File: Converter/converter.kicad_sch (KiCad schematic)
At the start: 0 parts

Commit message: added more flesh to overall structure, primarily on converter stage
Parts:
- added C10, C5, C6, C7, C8, C9, C_{bulk,in}, C_{bulk,out}: ~, symbol Device:C
- added L1: L, symbol Device:L
- added Q_{bottom}, Q_{top}: ~, symbol Transistor_FET:BSB013NE2LXI
- added R_{small,bottom}, R_{small,top}: R_small, symbol Device:R_US
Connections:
- new net +24V: C10.1, C8.1, C9.1, C_{bulk,out}.1, Q_{top}.1 (D)
- new net GNDPWR: C10.2, C5.2, C6.2, C7.2, C8.2, C9.2, C_{bulk,in}.2, C_{bulk,out}.2, Q_{bottom}.3 (S)
- new net HI_DRV: Q_{top}.2 (G), R_{small,top}.2
- new net LO_DRV: Q_{bottom}.2 (G), R_{small,bottom}.2
- new net V_{cap}: C5.1, C6.1, C7.1, C_{bulk,in}.1, L1.2
- new net V_{sw}: L1.1, Q_{bottom}.1 (D), Q_{top}.3 (S)
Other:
- note added: "Bidirectional Voltage Converter"
- note added: "Charging Critical Loop (minimize this!)"
- note added: "Charging decoupling caps"
- note added: "Discharging Critical Loop (minimize this!)"
- note added: "Discharging decoupling caps"
- note added: "Gate Driver Circuit"
- note added: "Low ESR"
- note added: "Test Points & Filters"

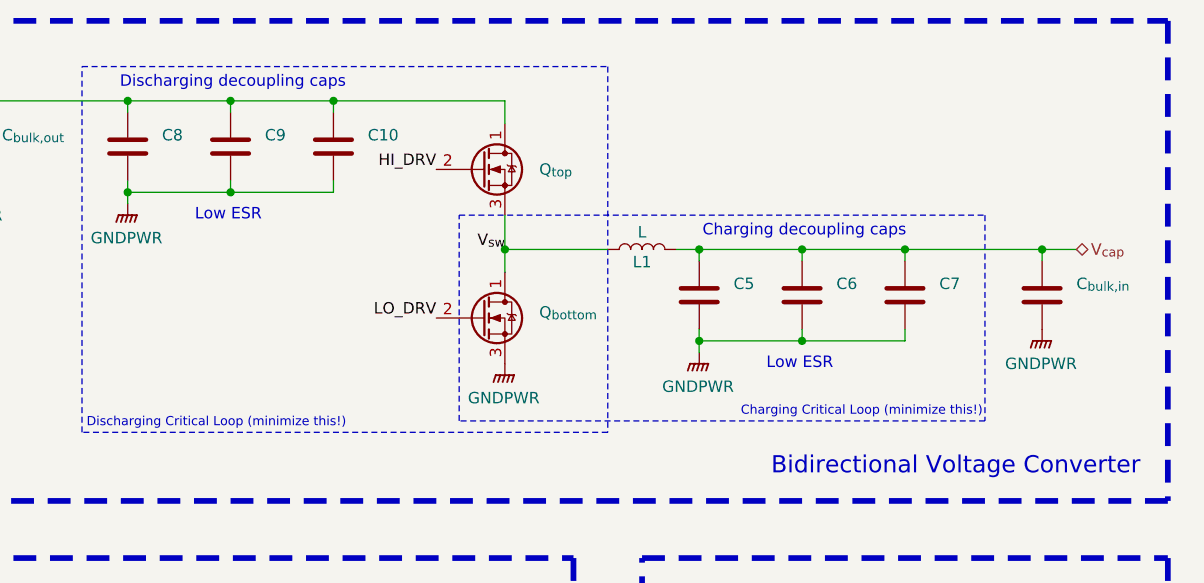
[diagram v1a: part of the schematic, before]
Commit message: removed unnecessary critical loop
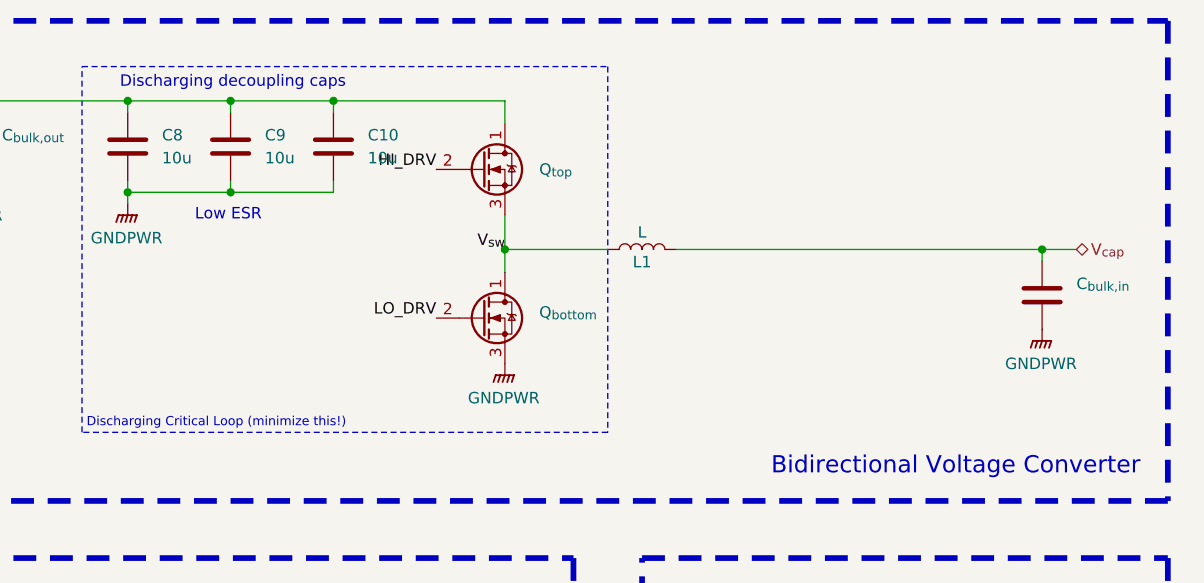
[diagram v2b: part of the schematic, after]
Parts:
- removed C5, C6, C7: ~, symbol Device:C
- C10, C8, C9: value ~ -> 10u
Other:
- note removed: "Charging Critical Loop (minimize this!)"
- note removed: "Charging decoupling caps"

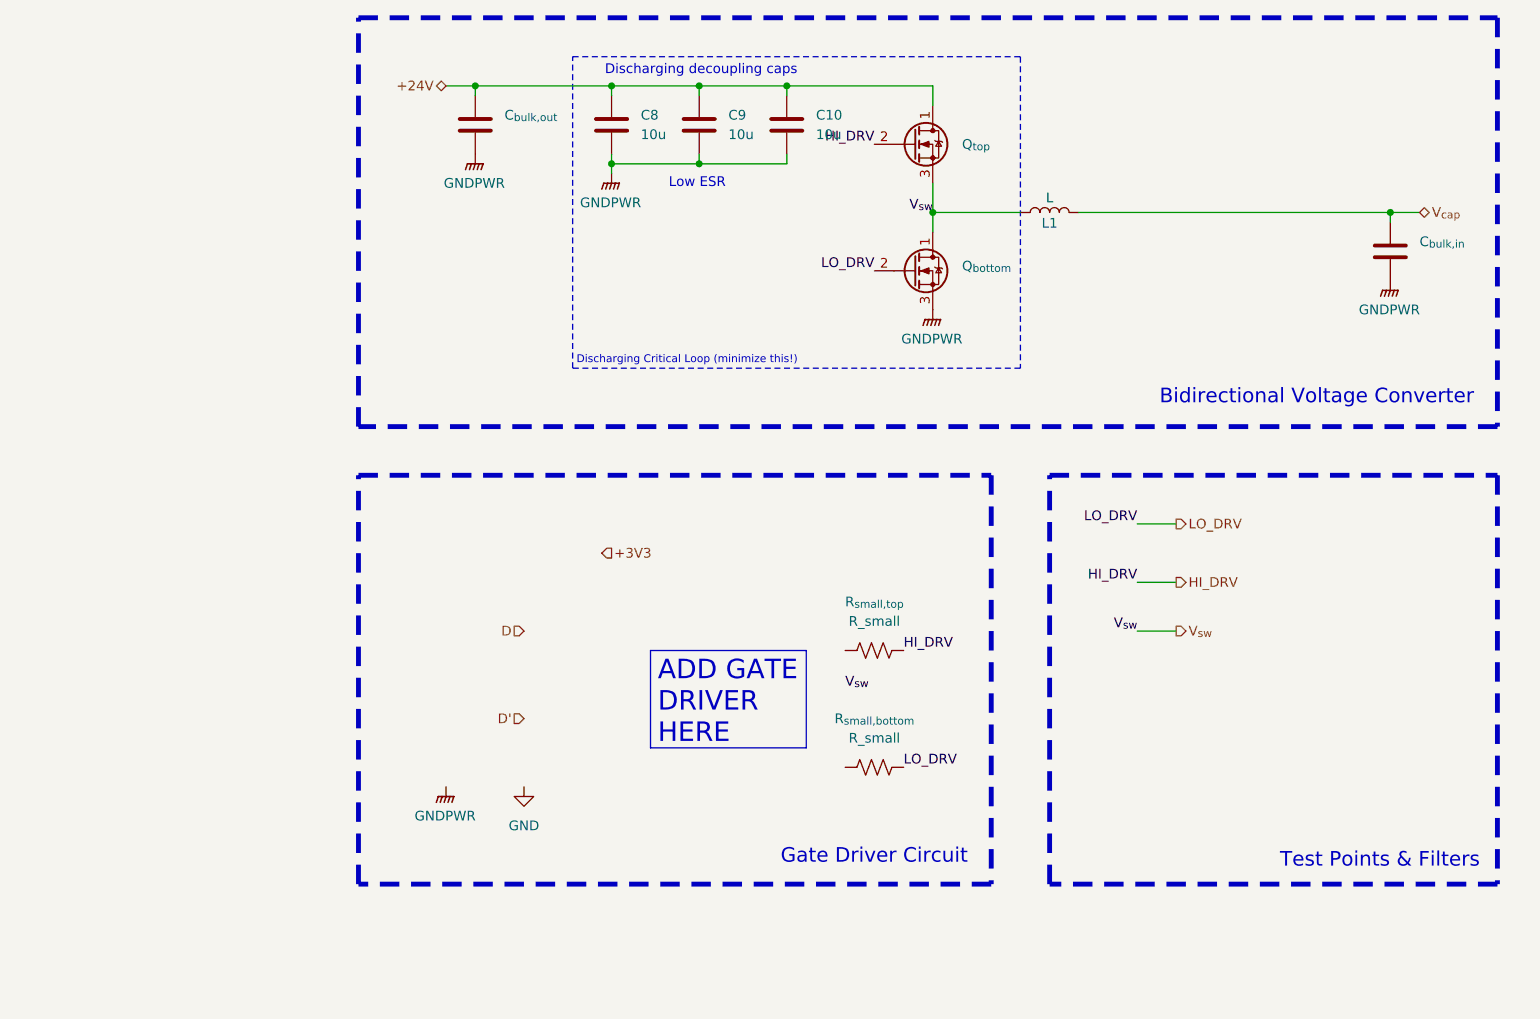
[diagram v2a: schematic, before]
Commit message: changed converter topology to full-bridge design
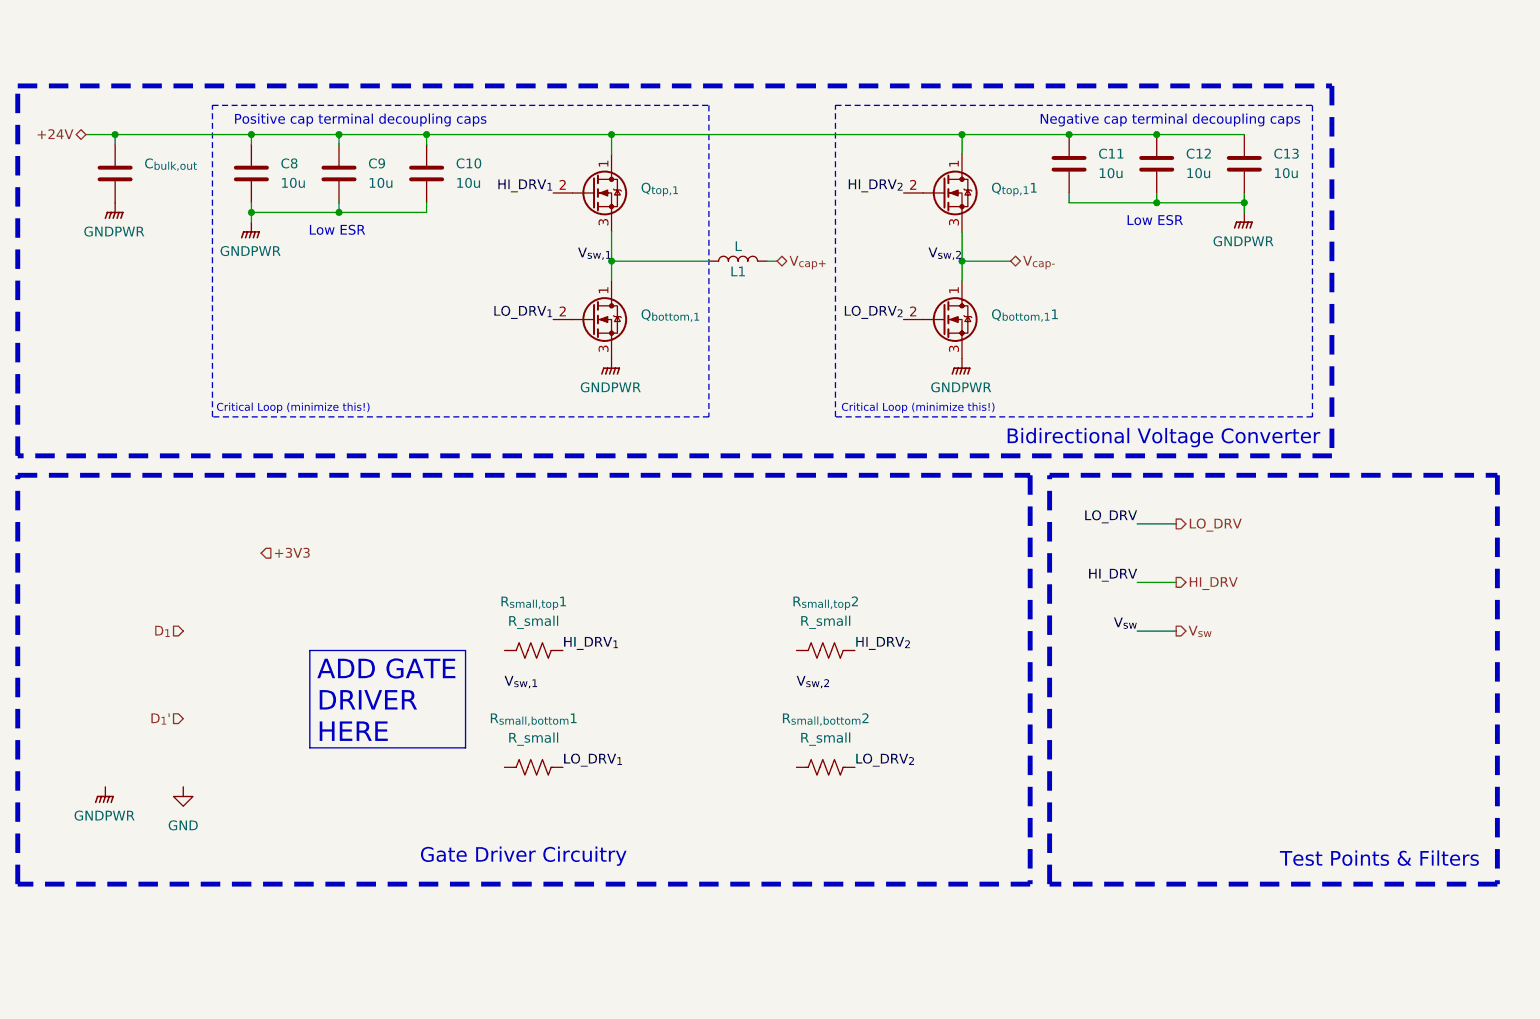
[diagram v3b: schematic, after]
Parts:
- removed C_{bulk,in}: ~, symbol Device:C
- added C11, C12, C13: 10u, symbol Device:C
- added Q_{bottom,1}1, Q_{top,1}1: ~, symbol Transistor_FET:BSB013NE2LXI
- added R_{small,bottom}2, R_{small,top}2: R_small, symbol Device:R_US
- renumbered Q_{bottom} to Q_{bottom,1}, Q_{top} to Q_{top,1}, R_{small,bottom} to R_{small,bottom}1, R_{small,top} to R_{small,top}1
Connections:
- net +24V: now also C11.1, C12.1, C13.1, Q_{top,1}1.1 (D)
- net GNDPWR: now also C11.2, C12.2, C13.2, Q_{bottom,1}1.3 (S)
- net HI_DRV: no longer Q_{top,1}.2 (G), R_{small,top}1.2
- net LO_DRV: no longer Q_{bottom,1}.2 (G), R_{small,bottom}1.2
- net V_{sw}: no longer L1.1, Q_{bottom,1}.1 (D), Q_{top,1}.3 (S)
- net V_{cap} renamed V_{cap+}
- new net HI_DRV_{1}: Q_{top,1}.2 (G), R_{small,top}1.2
- new net HI_DRV_{2}: Q_{top,1}1.2 (G), R_{small,top}2.2
- new net LO_DRV_{1}: Q_{bottom,1}.2 (G), R_{small,bottom}1.2
- new net LO_DRV_{2}: Q_{bottom,1}1.2 (G), R_{small,bottom}2.2
- new net V_{cap-}: Q_{bottom,1}1.1 (D), Q_{top,1}1.3 (S)
- new net V_{sw,1}: L1.1, Q_{bottom,1}.1 (D), Q_{top,1}.3 (S)
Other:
- note added: "Critical Loop (minimize this!)"
- note added: "Gate Driver Circuitry"
- note added: "Negative cap terminal decoupling caps"
- note added: "Positive cap terminal decoupling caps"
- note removed: "Discharging Critical Loop (minimize this!)"
- note removed: "Discharging decoupling caps"
- note removed: "Gate Driver Circuit"
- moved on the sheet: C10, C8, C9, C_{bulk,out}, L1, Q_{bottom,1}, Q_{top,1}, R_{small,bottom}1, R_{small,top}1

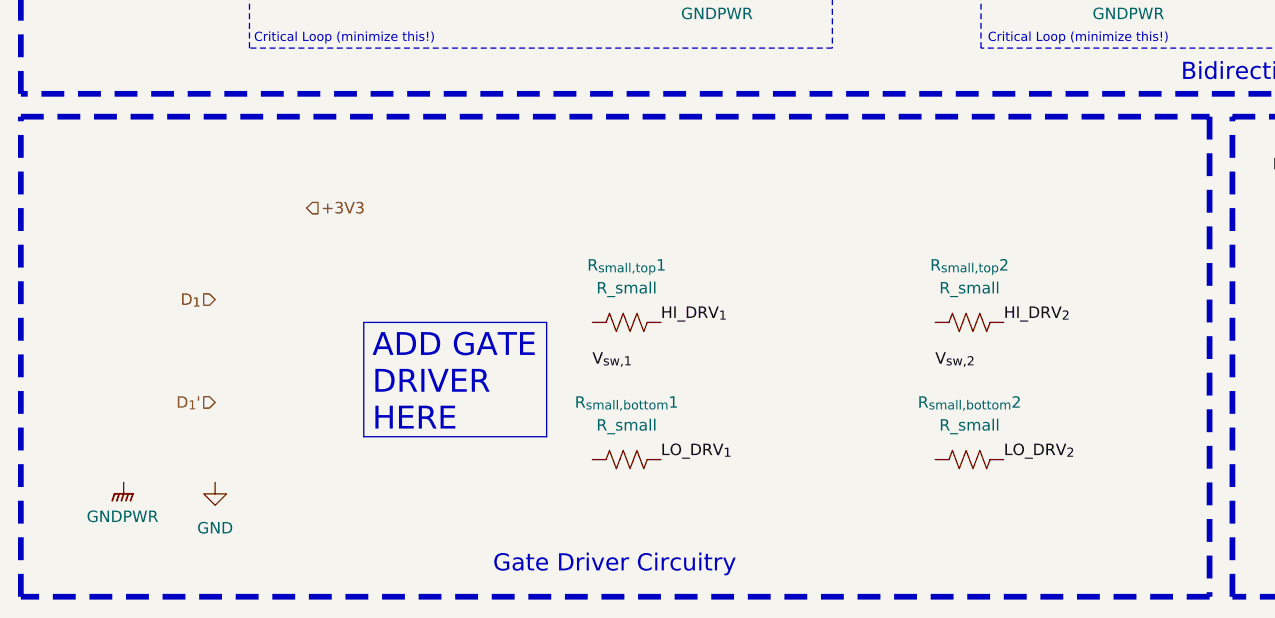
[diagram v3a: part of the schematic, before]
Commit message: began work on adding gate driver circuitry
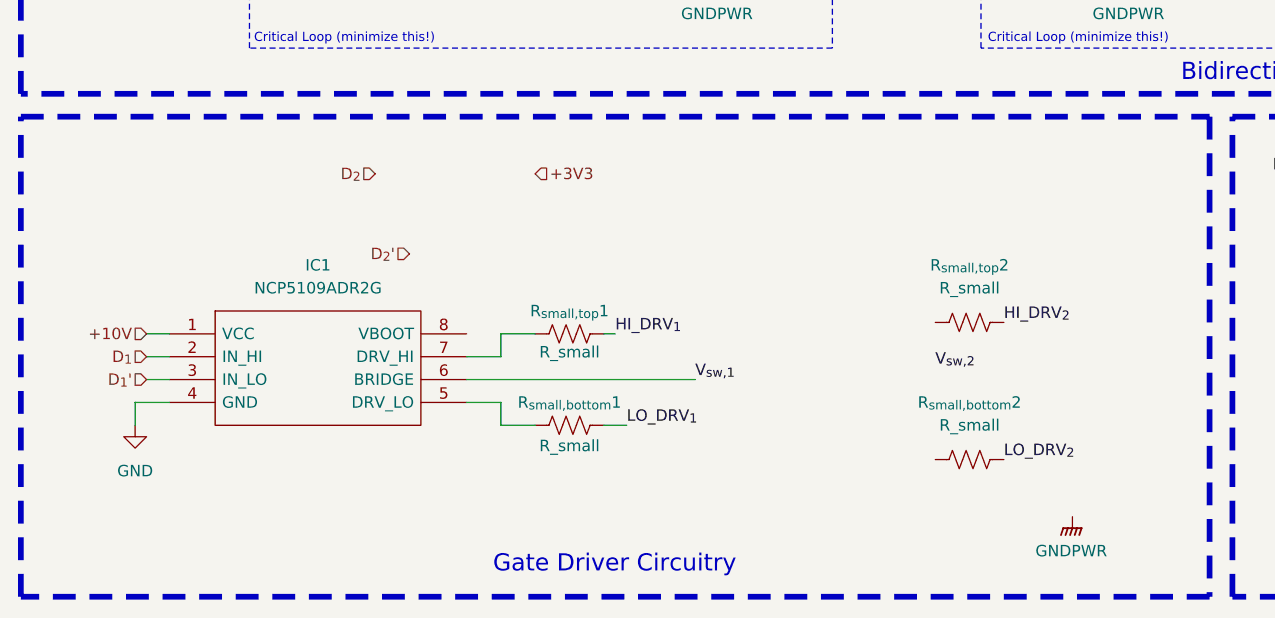
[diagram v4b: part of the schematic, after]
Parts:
- added IC1: NCP5109ADR2G, SOIC127P600X175-8N, symbol NCP5109ADR2G:NCP5109ADR2G
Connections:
- net D_{1}: now also IC1.2 (IN_HI)
- net D_{1}': now also IC1.3 (IN_LO)
- net GND: now also IC1.4 (GND)
- net V_{sw,1}: now also IC1.6 (BRIDGE)
- net at R_{small,top}1.1: now also IC1.7 (DRV_HI)
- net at R_{small,bottom}1.1: now also IC1.5 (DRV_LO)
- new net +10V: IC1.1 (VCC)
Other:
- moved on the sheet: R_{small,bottom}1, R_{small,top}1

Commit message: added symbol libraries and finished gate driver circuitry schematic
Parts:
- added C_{b}1, C_{b}2: 1u, Capacitor_SMD:C_0603_1608Metric_Pad1.08x0.95mm_HandSolder, symbol Device:C
- added C_{smooth}4, C_{smooth}5: 4.7u, Capacitor_SMD:C_0805_2012Metric_Pad1.18x1.45mm_HandSolder, symbol Device:C
- added D_{b}1, D_{b}2: D, Diode_SMD:D_MicroSMP_AK, symbol Device:D
- added IC2: NCP5109ADR2G, SOIC127P600X175-8N, symbol NCP5109ADR2G:NCP5109ADR2G
- added TP1, TP2, TP3, TP4, TP5, TP6: TestPoint, symbol Connector:TestPoint
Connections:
- net V_{sw,1} is gone; now on net V_{cap-}: IC1.6 (BRIDGE), L1.1, Q_{bottom,1}.1 (D), Q_{top,1}.3 (S)
- net +10V: now also IC1.8 (VBOOT), C_{smooth}4.1, C_{smooth}5.1, D_{b}1.2 (A), D_{b}2.2 (A), IC2.1 (VCC), IC2.8 (VBOOT)
- net D_{2}: now also IC2.2 (IN_HI)
- net D_{2}': now also IC2.3 (IN_LO)
- net GND: now also C_{smooth}4.2, C_{smooth}5.2, IC2.4 (GND)
- net HI_DRV_{1}: now also TP2.1
- net HI_DRV_{2}: now also TP5.1
- net LO_DRV_{1}: now also TP1.1
- net LO_DRV_{2}: now also TP4.1
- net V_{cap-}: now also C_{b}1.2, C_{b}2.2, IC2.6 (BRIDGE), TP3.1, TP6.1
- net at R_{small,top}2.1: now also IC2.7 (DRV_HI)
- net at R_{small,bottom}2.1: now also IC2.5 (DRV_LO)
- new net: C_{b}2.1, D_{b}2.1 (K)
- new net: C_{b}1.1, D_{b}1.1 (K)
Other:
- note added: "Outputs & Test Points"
- note removed: "Test Points & Filters"
- moved on the sheet: IC1, R_{small,bottom}1, R_{small,bottom}2, R_{small,top}1, R_{small,top}2

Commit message: added mosfet footprints and assigned to switch symbols
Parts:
- Q_{bottom,1}, Q_{bottom,1}1, Q_{top,1}, Q_{top,1}1: footprint (none) -> IQDH35N03LM5CGSCATMA1_MOSFET:IQDH45N04LM6CGSCATMA1
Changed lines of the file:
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@@
 			)
 		)
-		(property "Footprint" ""
+		(property "Footprint" "IQDH35N03LM5CGSCATMA1_MOSFET:IQDH45N04LM6CGSCATMA1"
 			(at 105.41 69.215 0)
 			(effects
@@
 			)
 		)
-		(property "Footprint" ""
+		(property "Footprint" "IQDH35N03LM5CGSCATMA1_MOSFET:IQDH45N04LM6CGSCATMA1"
 			(at 105.41 52.705 0)
 			(effects
@@
 			)
 		)
-		(property "Footprint" ""
+		(property "Footprint" "IQDH35N03LM5CGSCATMA1_MOSFET:IQDH45N04LM6CGSCATMA1"
 			(at 151.13 52.705 0)
 			(effects
@@
 			)
 		)
-		(property "Footprint" ""
+		(property "Footprint" "IQDH35N03LM5CGSCATMA1_MOSFET:IQDH45N04LM6CGSCATMA1"
 			(at 151.13 69.215 0)
 			(effects
